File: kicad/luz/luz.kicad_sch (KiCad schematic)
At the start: 71 parts, among them J1 Barrel_Jack, J2 U261-241N-4BS60, J3 Screw_Terminal_01x05, Q1 AO3400A, Q2 AO3400A, Q3 AO3400A, Q4 AO3400A, Q5 AOD413A, U1 STUSB4500QTR, U2 ESP32-S3, U3 W25Q16JVSSIQ, U4 SPX3819M5-L-3-3, Y1 40MHz

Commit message: Route DISCH pin through 1k resistor
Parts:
- added R15: 1k, Resistor_SMD:R_0402_1005Metric, symbol Device:R_Small
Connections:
- net +12V: now also R15.1
- net at U1.9 (DISCH): now also R15.2
- no-connect marks 42 -> 41
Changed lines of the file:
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@@
   (no_connect (at 48.895 55.245))
   (no_connect (at 227.33 140.97))
-  (no_connect (at 252.095 69.85))
   (no_connect (at 114.935 108.585))
   (no_connect (at 114.935 106.045))
@@
     (stroke (width 0) (type default))
   )
+  (wire (pts (xy 254.635 69.85) (xy 252.095 69.85))
+    (stroke (width 0) (type default))
+  )
   (wire (pts (xy 36.83 65.405) (xy 48.895 65.405))
     (stroke (width 0) (type default))
@@
     (stroke (width 0) (type default))
   )
+  (wire (pts (xy 264.16 73.025) (xy 254.635 73.025))
+    (stroke (width 0) (type default))
+  )
   (wire (pts (xy 33.655 136.525) (xy 45.72 136.525))
     (stroke (width 0) (type default))
@@
     (stroke (width 0) (type default))
   )
+  (wire (pts (xy 254.635 73.025) (xy 254.635 69.85))
+    (stroke (width 0) (type default))
+  )
   (wire (pts (xy 245.745 33.02) (xy 248.92 33.02))
     (stroke (width 0) (type default))
@@
     )
   )
+  (symbol (lib_id "Device:R_Small") (at 266.7 73.025 270) (mirror x) (unit 1)
+    (in_bom yes) (on_board yes) (dnp no)
+    (property "Reference" "R15" (at 266.7 75.565 90)
+      (effects (font (size 1.27 1.27)))
+    )
+    (property "Value" "1k" (at 266.7 78.105 90)
+      (effects (font (size 1.27 1.27)))
+    )
+    (property "Footprint" "Resistor_SMD:R_0402_1005Metric" (at 266.7 73.025 0)
+      (effects (font (size 1.27 1.27)) hide)
+    )
+    (property "Datasheet" "~" (at 266.7 73.025 0)
+      (effects (font (size 1.27 1.27)) hide)
+    )
+    (property "LCSC" "C11702" (at 266.7 73.025 90)
+      (effects (font (size 1.27 1.27)) hide)
+    )
+    (pin "1")
+    (pin "2")
+    (instances
+      (project "luz"
+        (path "/5e451c1d-8668-4fa5-842c-f16216d1b170"
+          (reference "R15") (unit 1)
+        )
+      )
+    )
+  )
   (symbol (lib_id "power:VBUS") (at 245.745 31.115 0) (unit 1)
     (in_bom yes) (on_board yes) (dnp no)
@@
         )
       )
+    )
+  )
+  (symbol (lib_id "power:+12V") (at 269.24 73.025 0) (unit 1)
+    (in_bom yes) (on_board yes) (dnp no) (fields_autoplaced)
+    (property "Reference" "#PWR047" (at 269.24 76.835 0)
+      (effects (font (size 1.27 1.27)) hide)
+    )
+    (property "Value" "+12V" (at 269.24 69.215 0)
+      (effects (font (size 1.27 1.27)))
+    )
+    (property "Footprint" "" (at 269.24 73.025 0)
+      (effects (font (size 1.27 1.27)) hide)
+    )
+    (property "Datasheet" "" (at 269.24 73.025 0)
+      (effects (font (size 1.27 1.27)) hide)
+    )
+    (pin "1")
+    (instances
+      (project "luz"
+        (path "/5e451c1d-8668-4fa5-842c-f16216d1b170"
+          (reference "#PWR047") (unit 1)
+        )
+      )

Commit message: Pull down RST from STUSB45, as suggested by datasheet
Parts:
- added R16: 10k, Resistor_SMD:R_0402_1005Metric, symbol Device:R_Small
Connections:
- net GND: now also R16.2
- net at U1.6 (RESET): now also R16.1
- no-connect marks 41 -> 40
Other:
- note added: "Can only handle +16V (+20 Absolute Max)."
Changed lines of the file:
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@@
   (no_connect (at 262.89 146.05))
   (no_connect (at 114.935 95.885))
-  (no_connect (at 221.615 49.53))
   (no_connect (at 114.935 67.945))
   (no_connect (at 114.935 73.025))
@@
     (stroke (width 0) (type default))
   )
+  (text "Can only handle +16V\n(+20 Absolute Max)." (at 101.6 137.16 0)
+    (effects (font (size 1.27 1.27)) (justify left bottom))
+  )
   (global_label "USBD-" (shape input) (at 266.7 135.89 0) (fields_autoplaced)
     (effects (font (size 1.27 1.27)) (justify left))
@@
     )
   )
+  (symbol (lib_id "power:GND") (at 216.535 49.53 0) (mirror y) (unit 1)
+    (in_bom yes) (on_board yes) (dnp no)
+    (property "Reference" "#PWR048" (at 216.535 55.88 0)
+      (effects (font (size 1.27 1.27)) hide)
+    )
+    (property "Value" "GND" (at 213.36 52.705 0)
+      (effects (font (size 1.27 1.27)))
+    )
+    (property "Footprint" "" (at 216.535 49.53 0)
+      (effects (font (size 1.27 1.27)) hide)
+    )
+    (property "Datasheet" "" (at 216.535 49.53 0)
+      (effects (font (size 1.27 1.27)) hide)
+    )
+    (pin "1")
+    (instances
+      (project "luz"
+        (path "/5e451c1d-8668-4fa5-842c-f16216d1b170"
+          (reference "#PWR048") (unit 1)
+        )
+      )
+    )
+  )
   (symbol (lib_id "power:+12V") (at 161.925 117.475 0) (unit 1)
     (in_bom yes) (on_board yes) (dnp no) (fields_autoplaced)
@@
         )
       )
+    )
+  )
+  (symbol (lib_id "Device:R_Small") (at 219.075 49.53 270) (unit 1)
+    (in_bom yes) (on_board yes) (dnp no)
+    (property "Reference" "R16" (at 220.98 46.99 90)
+      (effects (font (size 1.27 1.27)) (justify right))
+    )
+    (property "Value" "10k" (at 220.98 44.45 90)
+      (effects (font (size 1.27 1.27)) (justify right))
+    )
+    (property "Footprint" "Resistor_SMD:R_0402_1005Metric" (at 219.075 49.53 0)
+      (effects (font (size 1.27 1.27)) hide)
+    )
+    (property "Datasheet" "~" (at 219.075 49.53 0)
+      (effects (font (size 1.27 1.27)) hide)
+    )
+    (property "LCSC" "C25744" (at 219.075 49.53 90)
+      (effects (font (size 1.27 1.27)) hide)
+    )
+    (pin "1")
+    (pin "2")
+    (instances
+      (project "luz"
+        (path "/5e451c1d-8668-4fa5-842c-f16216d1b170"
+          (reference "R16") (unit 1)
+        )
+      )

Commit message: Added missing LCSC numbers
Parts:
- ANT1: LCSC (none) -> C293767
- D1, D2: LCSC (none) -> C3021136
- D3: LCSC (none) -> C72043
- D4, D6: LCSC (none) -> C2286
- J2: LCSC (none) -> C319150
- J3, TP1, TP10, TP2, TP3, TP4, TP5, TP6, TP9: now left out of the parts list
- Q5: LCSC (none) -> C115837
- U1: LCSC STUSB4500QTR -> C2678061
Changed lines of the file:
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@@
       (effects (font (size 1.27 1.27)) (justify bottom) hide)
     )
+    (property "LCSC" "C3021136" (at 205.74 121.92 0)
+      (effects (font (size 1.27 1.27)) hide)
+    )
     (pin "1")
     (pin "2")
@@
   )
   (symbol (lib_id "Connector:TestPoint") (at 149.225 31.75 270) (unit 1)
-    (in_bom yes) (on_board yes) (dnp no)
+    (in_bom no) (on_board yes) (dnp no)
     (property "Reference" "TP3" (at 154.813 31.115 90)
       (effects (font (size 1.27 1.27)) (justify left))
@@
   )
   (symbol (lib_id "Connector:TestPoint") (at 149.225 34.29 270) (unit 1)
-    (in_bom yes) (on_board yes) (dnp no)
+    (in_bom no) (on_board yes) (dnp no)
     (property "Reference" "TP4" (at 154.813 33.655 90)
       (effects (font (size 1.27 1.27)) (justify left))
@@
   )
   (symbol (lib_id "Connector:TestPoint") (at 149.225 26.035 270) (unit 1)
-    (in_bom yes) (on_board yes) (dnp no)
+    (in_bom no) (on_board yes) (dnp no)
     (property "Reference" "TP1" (at 154.813 25.4 90)
       (effects (font (size 1.27 1.27)) (justify left))
@@
   )
   (symbol (lib_id "Connector:TestPoint") (at 149.225 28.575 270) (unit 1)
-    (in_bom yes) (on_board yes) (dnp no)
+    (in_bom no) (on_board yes) (dnp no)
     (property "Reference" "TP2" (at 154.813 27.94 90)
       (effects (font (size 1.27 1.27)) (justify left))
@@
       (effects (font (size 1.27 1.27)) (justify bottom) hide)
     )
+    (property "LCSC" "C293767" (at 125.73 173.355 0)
+      (effects (font (size 1.27 1.27)) hide)
+    )
     (pin "1")
     (pin "2")
@@
       (effects (font (size 1.27 1.27)) hide)
     )
+    (property "LCSC" "C2286" (at 31.115 112.395 90)
+      (effects (font (size 1.27 1.27)) hide)
+    )
     (pin "1")
     (pin "2")
@@
       (effects (font (size 1.27 1.27)) (justify bottom) hide)
     )
+    (property "LCSC" "C115837" (at 259.08 35.56 90)
+      (effects (font (size 1.27 1.27)) hide)
+    )
     (pin "1")
     (pin "3")
@@
   )
   (symbol (lib_id "Connector:TestPoint") (at 150.495 52.07 270) (unit 1)
-    (in_bom yes) (on_board yes) (dnp no)
+    (in_bom no) (on_board yes) (dnp no)
     (property "Reference" "TP10" (at 156.083 51.435 90)
       (effects (font (size 1.27 1.27)) (justify left))
@@
       (effects (font (size 1.27 1.27)) (justify bottom) hide)
     )
+    (property "LCSC" "C319150" (at 245.11 138.43 0)
+      (effects (font (size 1.27 1.27)) hide)
+    )
     (pin "A1")
     (pin "A10")
@@
       (effects (font (size 1.27 1.27)) (justify bottom) hide)
     )
+    (property "LCSC" "C3021136" (at 208.915 149.86 90)
+      (effects (font (size 1.27 1.27)) hide)
+    )
     (pin "1")
     (pin "2")
@@
       (effects (font (size 1.27 1.27)) hide)
     )
+    (property "LCSC" "C72043" (at 263.525 61.595 90)
+      (effects (font (size 1.27 1.27)) hide)
+    )
     (pin "1")
     (pin "2")
@@
       (effects (font (size 1.27 1.27)) hide)
     )
+    (property "LCSC" "C2286" (at 274.32 61.595 90)
+      (effects (font (size 1.27 1.27)) hide)
+    )
     (pin "1")
     (pin "2")
@@
   )
   (symbol (lib_id "Connector:TestPoint") (at 149.225 22.86 270) (unit 1)
-    (in_bom yes) (on_board yes) (dnp no)
+    (in_bom no) (on_board yes) (dnp no)
     (property "Reference" "TP6" (at 154.813 22.225 90)
       (effects (font (size 1.27 1.27)) (justify left))
@@
       (effects (font (size 1.27 1.27)) hide)
     )
-    (property "LCSC" "STUSB4500QTR" (at 236.855 67.31 0)
+    (property "LCSC" "C2678061" (at 236.855 67.31 0)
       (effects (font (size 1.27 1.27)) hide)
     )
@@
   )
   (symbol (lib_id "Connector:TestPoint") (at 150.495 49.53 270) (unit 1)
-    (in_bom yes) (on_board yes) (dnp no)
+    (in_bom no) (on_board yes) (dnp no)
     (property "Reference" "TP9" (at 156.083 48.895 90)
       (effects (font (size 1.27 1.27)) (justify left))
@@
   )
   (symbol (lib_id "Connector:TestPoint") (at 149.225 37.465 270) (unit 1)
-    (in_bom yes) (on_board yes) (dnp no)
+    (in_bom no) (on_board yes) (dnp no)
     (property "Reference" "TP5" (at 154.813 36.83 90)
       (effects (font (size 1.27 1.27)) (justify left))
@@
   )
   (symbol (lib_id "Connector:Screw_Terminal_01x05") (at 170.815 81.28 90) (unit 1)
-    (in_bom yes) (on_board yes) (dnp no) (fields_autoplaced)
+    (in_bom no) (on_board yes) (dnp no) (fields_autoplaced)
     (property "Reference" "J3" (at 170.815 76.2 90)
       (effects (font (size 1.27 1.27)))

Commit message: Plotted files for production
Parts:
- TP7, TP8: now left out of the parts list
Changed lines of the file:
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@@
   )
   (symbol (lib_id "Connector:TestPoint") (at 164.465 120.015 270) (unit 1)
-    (in_bom yes) (on_board yes) (dnp no) (fields_autoplaced)
+    (in_bom no) (on_board yes) (dnp no) (fields_autoplaced)
     (property "Reference" "TP7" (at 170.18 119.38 90)
       (effects (font (size 1.27 1.27)) (justify left))
@@
   )
   (symbol (lib_id "Connector:TestPoint") (at 164.465 125.095 270) (unit 1)
-    (in_bom yes) (on_board yes) (dnp no) (fields_autoplaced)
+    (in_bom no) (on_board yes) (dnp no) (fields_autoplaced)
     (property "Reference" "TP8" (at 170.18 124.46 90)
       (effects (font (size 1.27 1.27)) (justify left))
@@
   )
   (symbol (lib_id "Connector:Screw_Terminal_01x05") (at 170.815 81.28 90) (unit 1)
-    (in_bom no) (on_board yes) (dnp no) (fields_autoplaced)
+    (in_bom no) (on_board no) (dnp no) (fields_autoplaced)
     (property "Reference" "J3" (at 170.815 76.2 90)
       (effects (font (size 1.27 1.27)))

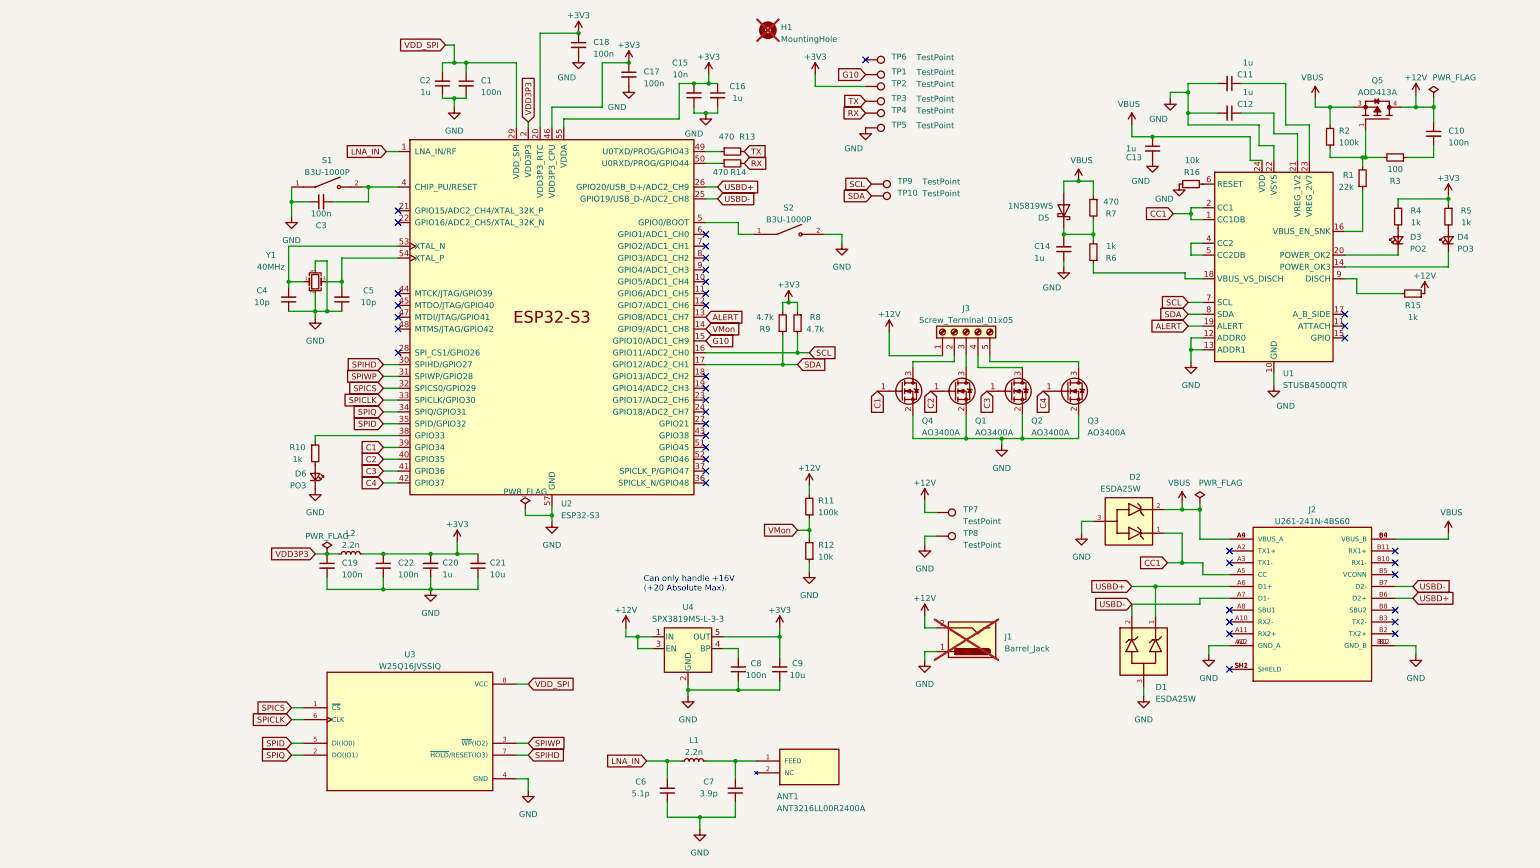
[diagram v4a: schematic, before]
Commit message: Routed new version with ESP32-WROOM
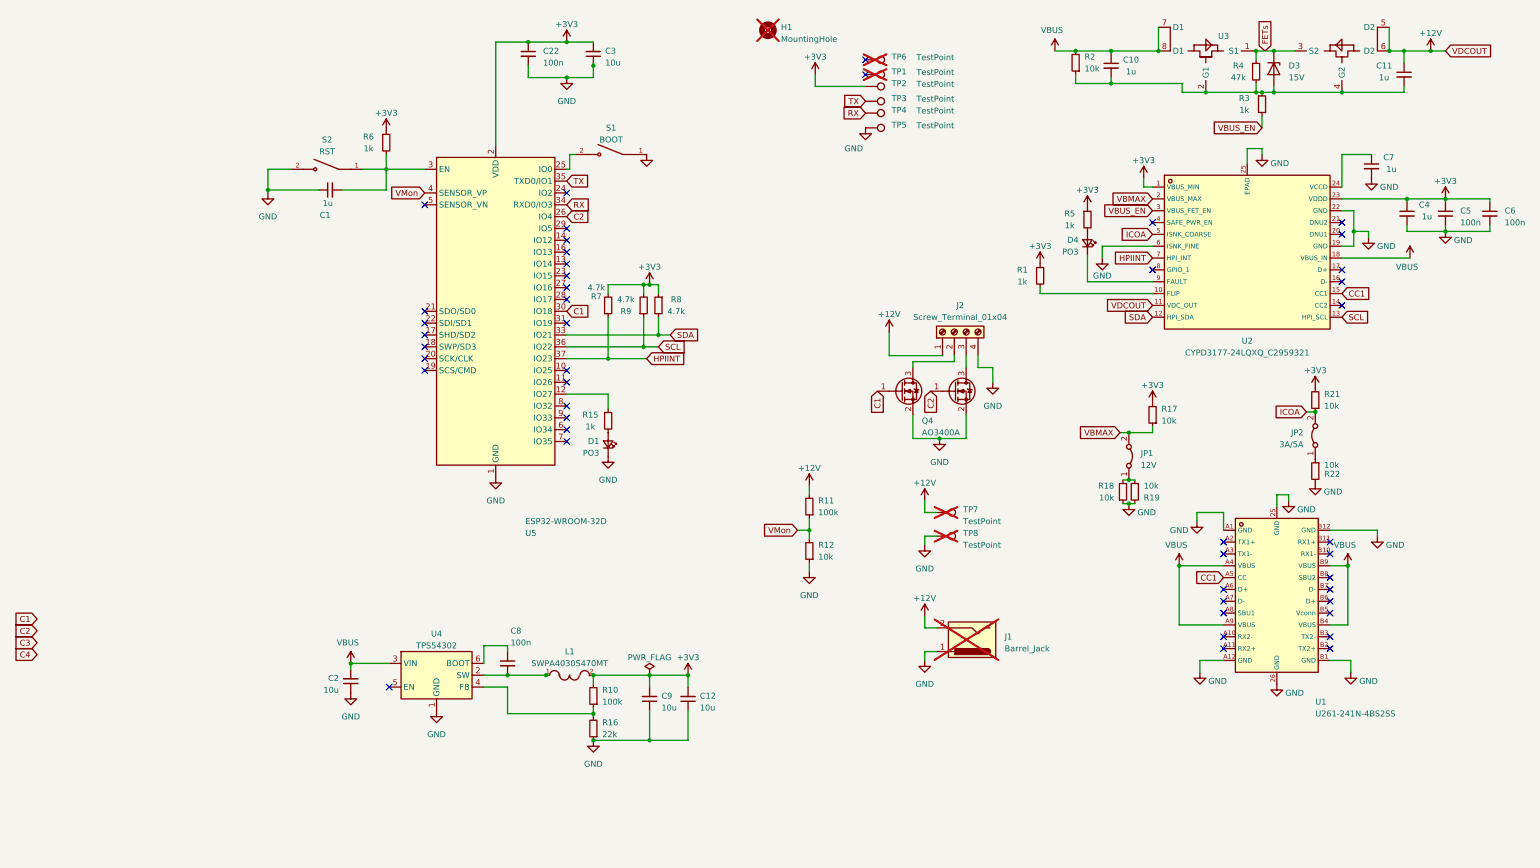
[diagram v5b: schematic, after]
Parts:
- removed ANT1: ANT3216LL00R2400A, Snapeda:ANTC3216X135N, symbol ANT3216LL00R2400A:ANT3216LL00R2400A
- removed C13, C14, C16, C20: 1u, Capacitor_SMD:C_0402_1005Metric, symbol Device:C_Small
- removed C15: 10n, Capacitor_SMD:C_0402_1005Metric, symbol Device:C_Small
- removed C17, C18, C19: 100n, Capacitor_SMD:C_0402_1005Metric, symbol Device:C_Small
- removed C21: 10u, Capacitor_SMD:C_0402_1005Metric, symbol Device:C_Small
- removed D1, D2: ESDA25W, Snapeda:SOT65P210X110-3N, symbol ESDA25W:ESDA25W
- removed D3: PO2, LED_SMD:LED_0603_1608Metric, symbol Device:LED_Small
- removed D5: 1N5819WS, Diode_SMD:D_SOD-323, symbol Diode:1N5819WS
- removed D6: PO3, LED_SMD:LED_0603_1608Metric, symbol Device:LED_Small
- removed J2: U261-241N-4BS60, Snapeda:XKB_U261-241N-4BS60, symbol U261-241N-4BS60:U261-241N-4BS60
- removed J3: Screw_Terminal_01x05, TerminalBlock_Phoenix:TerminalBlock_Phoenix_MKDS-1,5-5-5.08_1x05_P5.08mm_Horizontal, symbol Connector:Screw_Terminal_01x05
- removed L1, L2: 2.2n, Inductor_SMD:L_0402_1005Metric, symbol Device:L_Small
- removed Q2, Q3: AO3400A, Package_TO_SOT_SMD:SOT-23, symbol Transistor_FET:AO3400A
- removed Q5: AOD413A, Snapeda:TRANS_AOD413A, symbol AOD413A:AOD413A
- removed R13, R14: 470, Resistor_SMD:R_0402_1005Metric, symbol Device:R_Small
- removed TP10, TP9: TestPoint, TestPoint:TestPoint_Pad_D1.5mm, symbol Connector:TestPoint
- removed U1: STUSB4500QTR, Package_DFN_QFN:QFN-24-1EP_4x4mm_P0.5mm_EP2.7x2.7mm, symbol Interface_USB:STUSB4500QTR
- removed U2: ESP32-S3, Package_DFN_QFN:QFN-56-1EP_7x7mm_P0.4mm_EP5.6x5.6mm, symbol PCM_Espressif:ESP32-S3
- removed U3: W25Q16JVSSIQ, Snapeda:SOIC127P790X216-8N, symbol W25Q16JVSSIQ:W25Q16JVSSIQ
- removed U4: SPX3819M5-L-3-3, Package_TO_SOT_SMD:SOT-23-5, symbol Regulator_Linear:SPX3819M5-L-3-3
- removed Y1: 40MHz, Crystal:Crystal_SMD_2520-4Pin_2.5x2.0mm, symbol Device:Crystal_GND24_Small
- added D1: PO3, LED_SMD:LED_0603_1608Metric, symbol Device:LED_Small
- added D3: 15V, Diode_SMD:D_SOD-323, symbol Device:D_Zener
- added J2: Screw_Terminal_01x04, TerminalBlock_Phoenix:TerminalBlock_Phoenix_MKDS-1,5-4_1x04_P5.00mm_Horizontal, symbol Connector:Screw_Terminal_01x04
- added JP1: 12V, Jumper:SolderJumper-2_P1.3mm_Bridged_RoundedPad1.0x1.5mm, symbol Jumper:Jumper_2_Bridged
- added JP2: 3A/5A, Jumper:SolderJumper-2_P1.3mm_Bridged_RoundedPad1.0x1.5mm, symbol Jumper:Jumper_2_Bridged
- added L1: SWPA4030S470MT, footprint:IND-SMD_L4.0-W4.0_SLS3DXX, symbol SWPA4030S470MT:SWPA4030S470MT
- added R17, R18, R19, R21, R22: 10k, Resistor_SMD:R_0402_1005Metric, symbol Device:R_Small
- added U1: U261-241N-4BS2SS, footprint:USB-C-SMD_U261-241N-4BS2SS, symbol U261-241N-4BS2SS:U261-241N-4BS2SS
- added U2: CYPD3177-24LQXQ_C2959321, footprint:TQFN-24_L4.0-W4.0-P0.50-TL-EP2.8, symbol CYPD3177-24LQXQ_C2959321:CYPD3177-24LQXQ_C2959321
- added U3: ~, footprint:SO-8_L4.9-W3.9-P1.27-LS5.9-BL, symbol SI4909DY-T1-GE3:Test
- added U4: TPS54302, Package_TO_SOT_SMD:SOT-23-6, symbol Regulator_Switching:TPS54302
- added U5: ESP32-WROOM-32D, RF_Module:ESP32-WROOM-32D, symbol RF_Module:ESP32-WROOM-32D
- C1, C10: value 100n -> 1u; LCSC C77020 -> C52923
- C12, C2: value 1u -> 10u; footprint Capacitor_SMD:C_0402_1005Metric -> Capacitor_SMD:C_0603_1608Metric; LCSC C52923 -> C194427
- C3: value 100n -> 10u; footprint Capacitor_SMD:C_0402_1005Metric -> Capacitor_SMD:C_0603_1608Metric; LCSC C77020 -> C194427
- C4: value 10p -> 1u; LCSC C106199 -> C52923
- C5: value 10p -> 100n; LCSC C106199 -> C77020
- C6: value 5.1p -> 100n; LCSC C541354 -> C77020
- C7: value 3.9p -> 1u; LCSC C505474 -> C52923
- C9: footprint Capacitor_SMD:C_0402_1005Metric -> Capacitor_SMD:C_0603_1608Metric; LCSC C15525 -> C194427
- R1: value 22k -> 1k; LCSC C25768 -> C11702
- R10: value 1k -> 100k; LCSC C11702 -> C25741
- R16: value 10k -> 22k; LCSC C25744 -> C25768
- R2: value 100k -> 10k; LCSC C25741 -> C25744
- R3: value 100 -> 1k; LCSC C2935235 -> C11702
- R4: value 1k -> 47k; LCSC C11702 -> C25792
- R7: value 470 -> 4.7k; LCSC C25117 -> C25900
- S1: value B3U-1000P -> BOOT
- S2: value B3U-1000P -> RST
- TP1, TP6, TP7, TP8: now not fitted
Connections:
- net LNA_IN is gone; now on net GND: C6.2
- net +12V: now also C11.1, J2.1 (Pin_1), U2.11 (VDC_OUT), U3.5 (D2), U3.6 (D2); no longer C10.1, R15.1
- net +3V3: now also C12.2, C3.2, C4.1, C5.1, C6.1, R1.1, R10.2, R6.1, R7.2, L1.2, R17.2, R21.2, U2.1 (VBUS_MIN), U2.23 (VDDD), U5.2 (VDD); no longer R4.1
- net C1: now also U5.30 (IO18)
- net C2: now also U5.26 (IO4)
- net CC1: now also U1.A5 (CC), U2.15 (CC1)
- net GND: now also C1.1, C12.1, C4.2, C5.2, C7.2, R16.1, D1.1 (K), J2.4 (Pin_4), R18.1, R19.2, R22.2, U1.25 (GND), U1.26 (GND), U1.A1 (GND), U1.A12 (GND), U1.B1 (GND), U1.B12 (GND), U2.19 (GND), U2.22 (GND), U2.25 (EPAD), U2.6 (ISNK_FINE), U4.1 (GND), U5.1 (GND), U5.15 (GND), U5.38 (GND), U5.39 (GND); no longer C1.2, C11.2, C12.2, C4.1, C5.1, C6.1, C7.1, C8.1, R16.2
- net RX: now also U5.34 (RXD0/IO3)
- net SCL: now also R9.1, U2.13 (HPI_SCL), U5.36 (IO22); no longer R8.2
- net SDA: now also R8.2, U2.12 (HPI_SDA), U5.33 (IO21); no longer R9.1
- net TX: now also U5.35 (TXD0/IO1)
- net VBUS: now also C10.1, C2.2, U1.A4 (VBUS), U1.A9 (VBUS), U1.B4 (VBUS), U1.B9 (VBUS), U2.18 (VBUS_IN), U3.7 (D1), U3.8 (D1), U4.3 (VIN); no longer R7.1
- net VMon: now also U5.4 (SENSOR_VP)
- net at S2.1: now also C1.2, R6.2, U5.3 (EN)
- net at Q1.3 (D): now also J2.3 (Pin_3)
- net at S1.2: now also U5.25 (IO0); no longer C3.2
- net at R10.1: now also R16.2, U4.4 (FB)
- net at C8.2: now also L1.1, U4.2 (SW)
- net at C10.2, R3.1: now also C11.2, R2.1, R4.2, D3.2 (A), U3.2 (G1), U3.4 (G2)
- net at Q4.3 (D): now also J2.2 (Pin_2)
- net at D4.1 (K): now also U2.9 (FAULT)
- net at R15.2: now also D1.2 (A)
- net G10: no longer names the net of TP1.1
- removed net VDD_SPI: C1.1, C2.2
- new net: C8.1, U4.6 (BOOT)
- new net: JP2.1 (A), R22.1
- new net: R15.1, U5.12 (IO27)
- new net: C7.1, U2.24 (VCCD)
- new net: JP1.1 (A), R18.2, R19.1
- new net: R1.2, U2.10 (FLIP)
- new net FETs: D3.1 (K), R4.1, U3.1 (S1), U3.3 (S2)
- new net HPIINT: R7.1, U2.7 (HPI_INT), U5.37 (IO23)
- new net ICOA: JP2.2 (B), R21.1, U2.5 (ISNK_COARSE)
- new net VBMAX: JP1.2 (B), R17.1, U2.2 (VBUS_MAX)
- new net VBUS_EN: R3.2, U2.3 (VBUS_FET_EN)
- no-connect marks 40 -> 47
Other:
- note removed: "Can only handle +16V (+20 Absolute Max)."
- moved on the sheet: C22, D4, R5, R8, R9, S1, S2

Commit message: Fix schematic DRC
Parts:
- J2: now left out of the parts list
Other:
- moved on the sheet: JP2, R21, R22, U1
